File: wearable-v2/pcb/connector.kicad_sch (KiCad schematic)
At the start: 38 parts, among them J1 EXT_1, J11 PNL_1, J12 PNL_2, J13 PNL_3, J14 PNL_4, J2 EXT_2, J3 EXT_3, J4 EXT_4, J7 USB_C_Receptacle_USB2.0, U1 DT1446-04V, U15 TLV751, U2 MCP73831/2-2MC, U3 TCA6408A, U4 FT201XQ

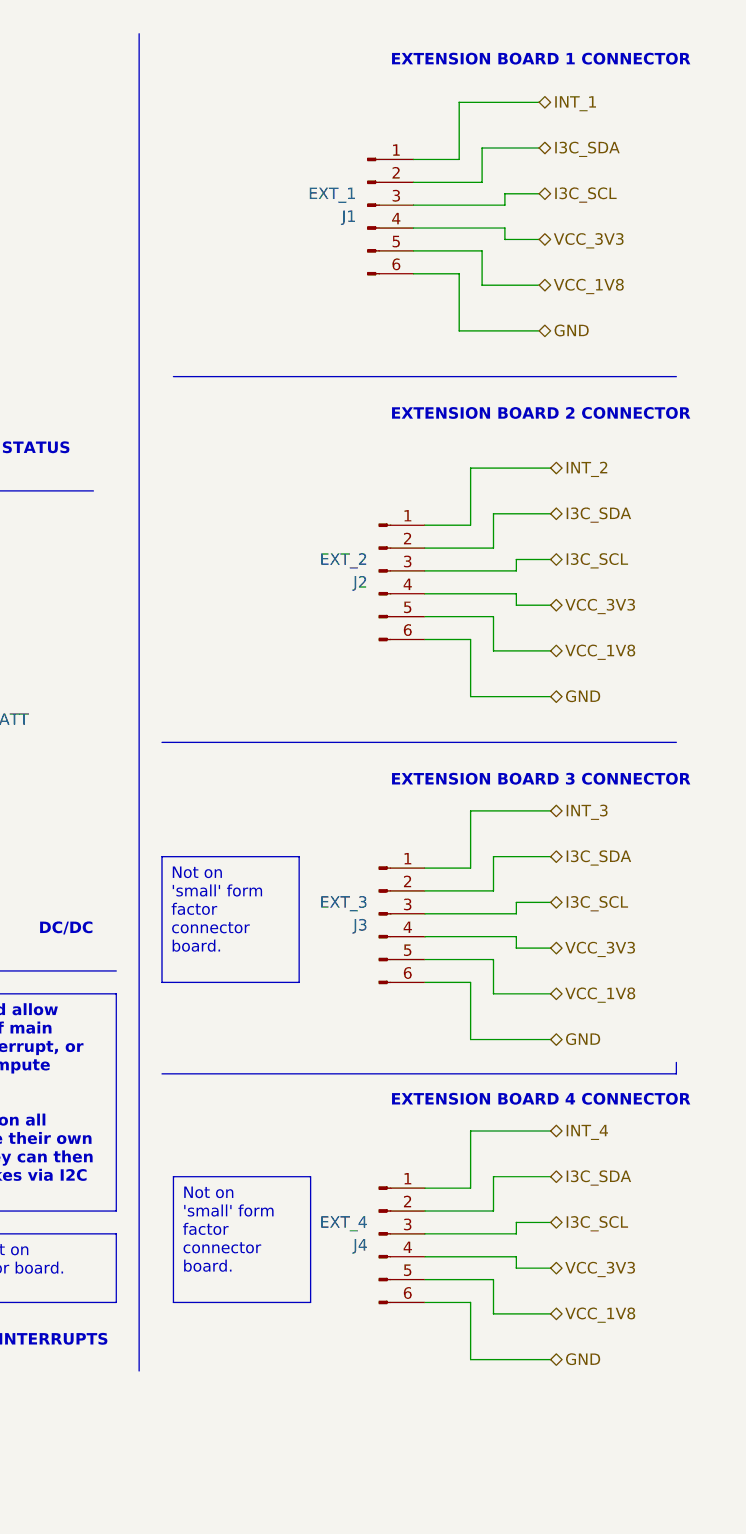
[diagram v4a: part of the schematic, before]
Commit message: Added front connectors on main board
Signed-off-by: Adam Fowler <adam@adamfowler.org>
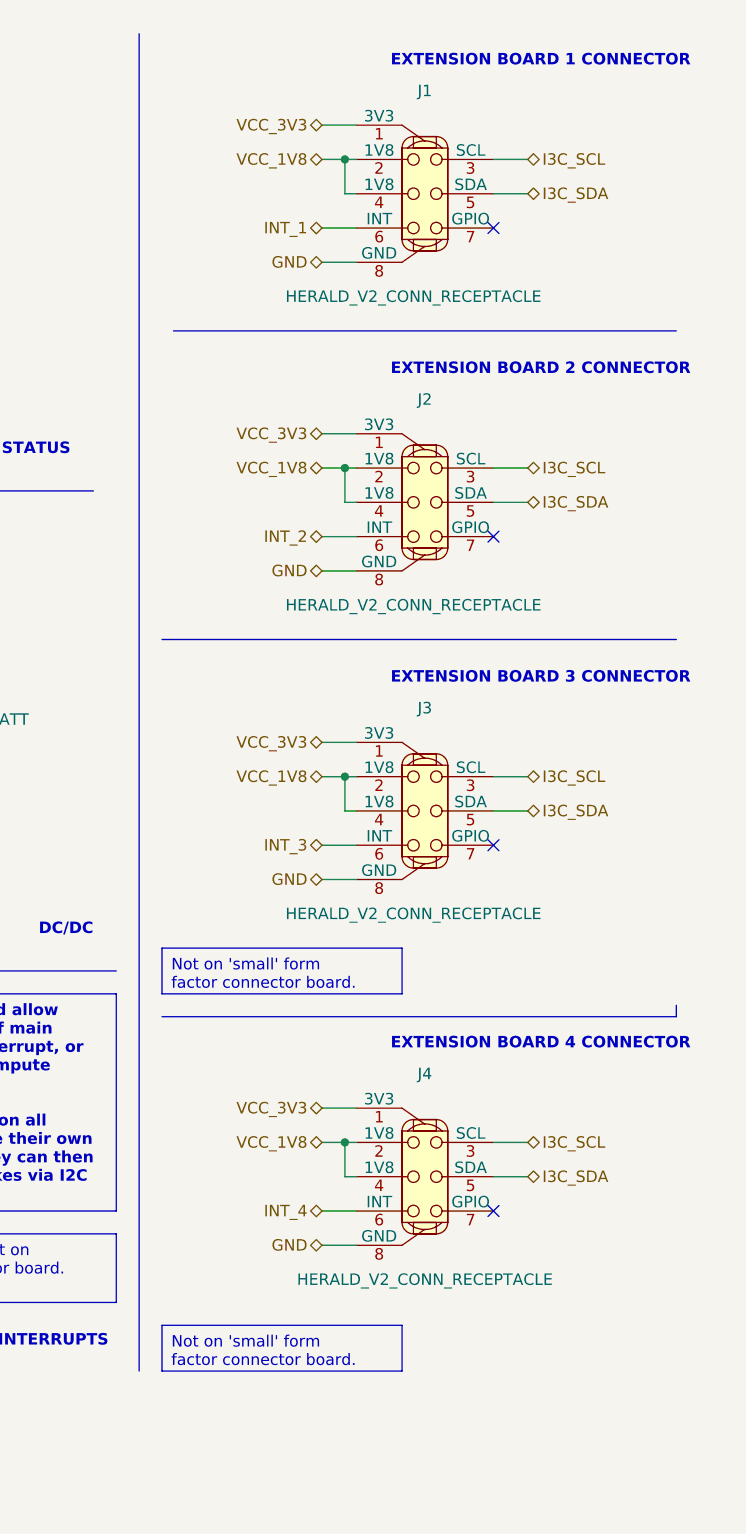
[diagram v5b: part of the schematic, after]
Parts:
- removed J1: EXT_1, symbol Connector:Conn_01x06_Pin
- removed J2: EXT_2, symbol Connector:Conn_01x06_Pin
- removed J3: EXT_3, symbol Connector:Conn_01x06_Pin
- removed J4: EXT_4, symbol Connector:Conn_01x06_Pin
- added J1, J2, J3, J4: HERALD_V2_CONN_RECEPTACLE, Herald:HERALD_V2_CONN_RECEPTACLE, symbol Herald_Extras:HERALD_V2_CONN_RECEPTACLE
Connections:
- net +1V8: now also J1.2 (1V8), J1.4 (1V8), J2.2 (1V8), J2.4 (1V8), J3.2 (1V8), J3.4 (1V8), J4.2 (1V8), J4.4 (1V8)
- net GND: now also J1.8 (GND), J2.8 (GND), J3.8 (GND), J4.8 (GND)
- net I3C_SCL: now also J1.3 (SCL), J2.3 (SCL), J3.3 (SCL), J4.3 (SCL)
- net I3C_SDA: now also J1.5 (SDA), J2.5 (SDA), J3.5 (SDA), J4.5 (SDA)
- net INT_1: now also J1.6 (INT)
- net INT_2: now also J2.6 (INT)
- net INT_3: now also J3.6 (INT)
- net INT_4: now also J4.6 (INT)
- net VDD: now also J1.1 (3V3), J2.1 (3V3), J3.1 (3V3), J4.1 (3V3)
- no-connect marks 13 -> 17

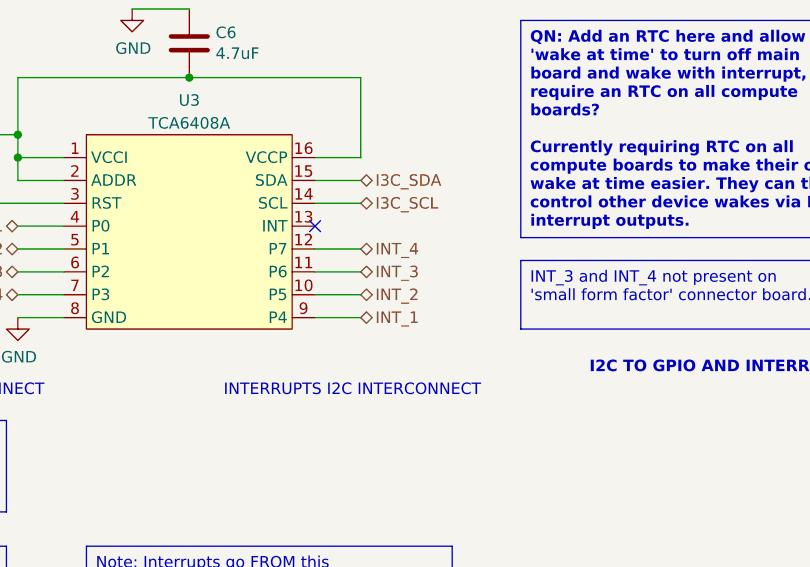
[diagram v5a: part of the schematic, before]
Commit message: All board connectors routed
Connector positions confirmed
Extension board dimensions confirmed to not clash
Signed-off-by: Adam Fowler <adam@adamfowler.org>
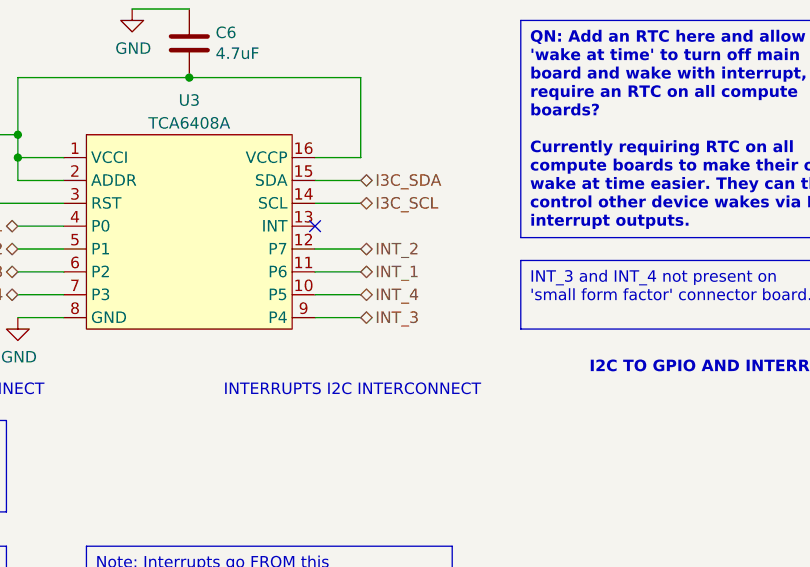
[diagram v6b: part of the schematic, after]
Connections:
- net INT_1: now also U3.11 (P6); no longer U3.9 (P4)
- net INT_2: now also U3.12 (P7); no longer U3.10 (P5)
- net INT_3: now also U3.9 (P4); no longer U3.11 (P6)
- net INT_4: now also U3.10 (P5); no longer U3.12 (P7)
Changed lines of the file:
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@@
+    (stroke (width 0) (type default))
+  )
+  (wire (pts (xy 158.75 149.86) (xy 163.83 149.86))
     (stroke (width 0) (type default))
   )
@@
     (stroke (width 0) (type default))
   )
+  (wire (pts (xy 158.75 154.94) (xy 163.83 154.94))
+    (stroke (width 0) (type default))
+  )
   (wire (pts (xy 33.02 153.67) (xy 31.75 153.67))
     (stroke (width 0) (type default))
@@
     (stroke (width 0) (type default))
   )
+  (wire (pts (xy 158.75 147.32) (xy 163.83 147.32))
+    (stroke (width 0) (type default))
+  )
   (wire (pts (xy 129.54 99.06) (xy 129.54 96.52))
     (stroke (width 0) (type default))
@@
     (stroke (width 0) (type default))
   )
-  (wire (pts (xy 158.75 147.32) (xy 163.83 147.32))
-    (stroke (width 0) (type default))
-  )
   (wire (pts (xy 76.2 97.79) (xy 76.2 99.06))
     (stroke (width 0) (type default))
@@
     (stroke (width 0) (type default))
   )
-  (wire (pts (xy 158.75 154.94) (xy 163.83 154.94))
-    (stroke (width 0) (type default))
-  )
   (wire (pts (xy 27.94 77.47) (xy 25.4 77.47))
     (stroke (width 0) (type default))
@@
     (stroke (width 0) (type default))
   )
+  (wire (pts (xy 158.75 152.4) (xy 163.83 152.4))
+    (stroke (width 0) (type default))
+  )
   (wire (pts (xy 245.11 63.5) (xy 246.38 63.5))
     (stroke (width 0) (type default))
@@
     (stroke (width 0) (type default))
   )
-  (wire (pts (xy 158.75 152.4) (xy 163.83 152.4))
-    (stroke (width 0) (type default))
-  )
   (wire (pts (xy 15.24 134.62) (xy 33.02 134.62))
     (stroke (width 0) (type default))
@@
   )
   (wire (pts (xy 158.75 87.63) (xy 158.75 88.9))
-    (stroke (width 0) (type default))
-  )
-  (wire (pts (xy 158.75 149.86) (xy 163.83 149.86))
     (stroke (width 0) (type default))
   )
@@
     (effects (font (size 1.27 1.27)) (justify left))
   )
-  (hierarchical_label "INT_1" (shape bidirectional) (at 163.83 154.94 0) (fields_autoplaced)
+  (hierarchical_label "INT_1" (shape bidirectional) (at 163.83 149.86 0) (fields_autoplaced)
     (effects (font (size 1.27 1.27)) (justify left))
   )
@@
     (effects (font (size 1.27 1.27)) (justify left))
   )
-  (hierarchical_label "INT_3" (shape bidirectional) (at 163.83 149.86 0) (fields_autoplaced)
+  (hierarchical_label "INT_3" (shape bidirectional) (at 163.83 154.94 0) (fields_autoplaced)
     (effects (font (size 1.27 1.27)) (justify left))
   )
@@
     (effects (font (size 1.27 1.27)) (justify left))
   )
-  (hierarchical_label "INT_4" (shape bidirectional) (at 163.83 147.32 0) (fields_autoplaced)
+  (hierarchical_label "INT_4" (shape bidirectional) (at 163.83 152.4 0) (fields_autoplaced)
     (effects (font (size 1.27 1.27)) (justify left))
   )
@@
     (effects (font (size 1.27 1.27)) (justify left))
   )
-  (hierarchical_label "INT_2" (shape bidirectional) (at 163.83 152.4 0) (fields_autoplaced)
-    (effects (font (size 1.27 1.27)) (justify left))
-  )
+  (hierarchical_label "INT_2" (shape bidirectional) (at 163.83 147.32 0) (fields_autoplaced)
+    (effects (font (size 1.27 1.27)) (justify left))
+  )

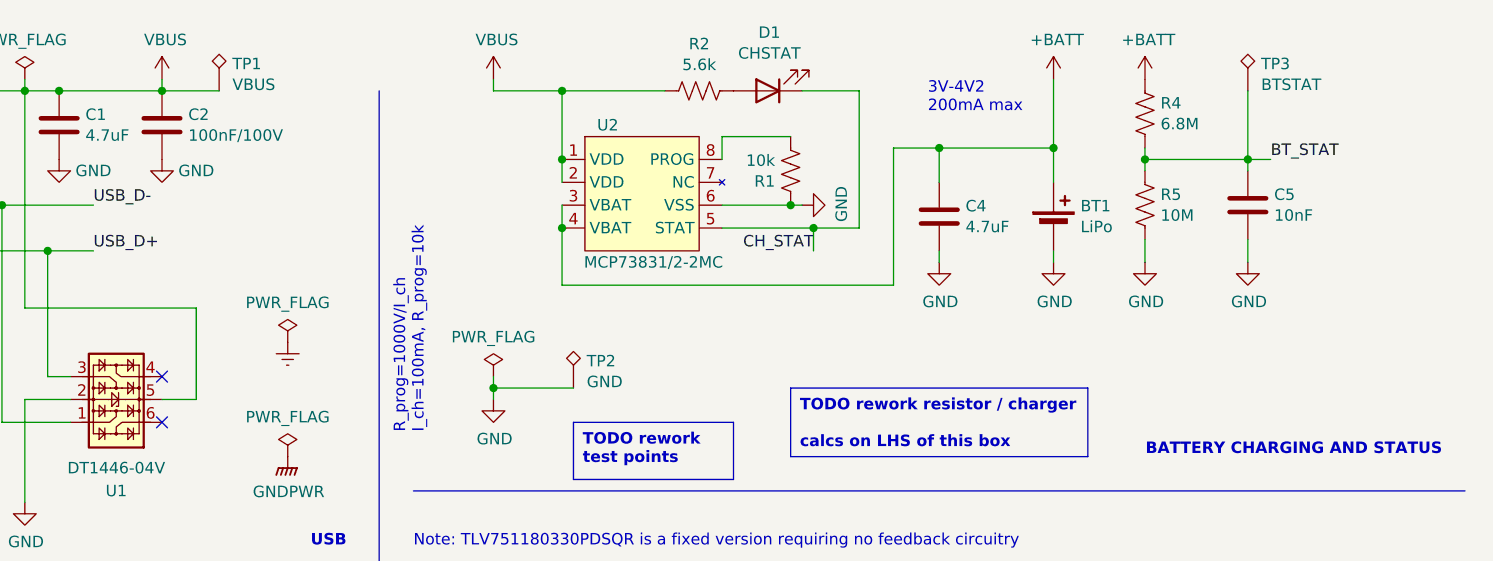
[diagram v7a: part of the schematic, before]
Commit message: Set wider PCB GND tracks and vias
Signed-off-by: Adam Fowler <adam@adamfowler.org>
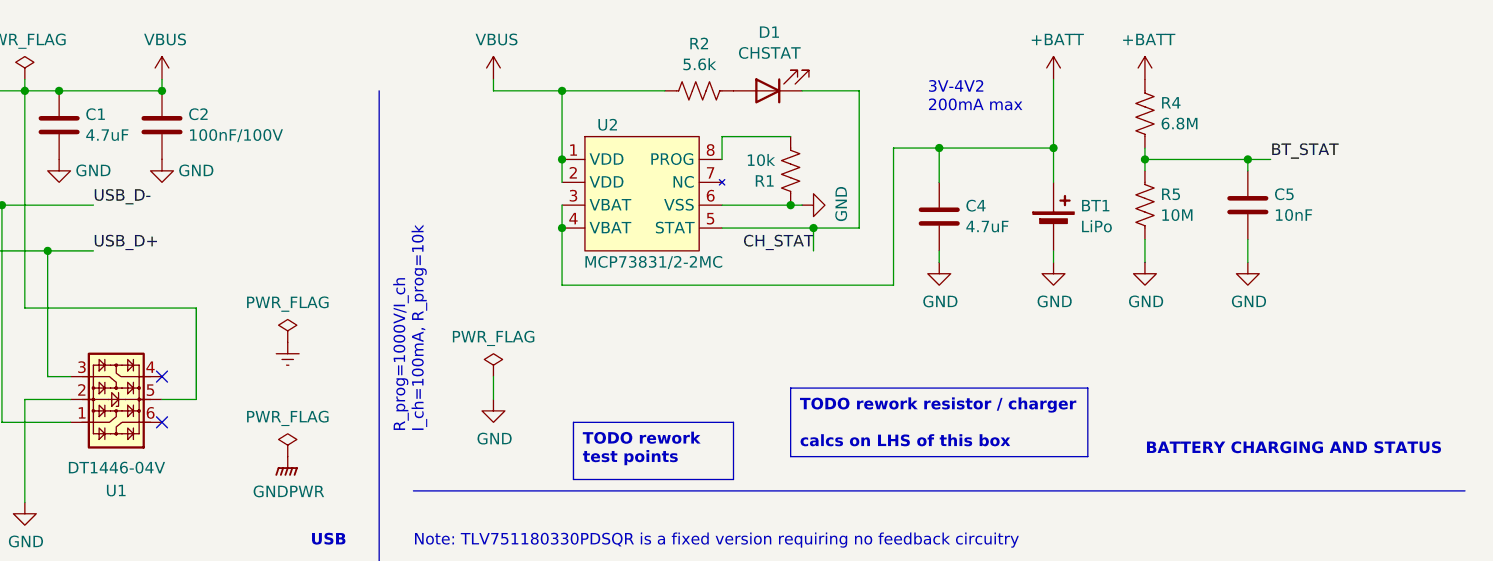
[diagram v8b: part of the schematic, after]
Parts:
- removed TP1: VBUS, TestPoint:TestPoint_Pad_D1.0mm, symbol Connector:TestPoint_Alt
- removed TP2: GND, TestPoint:TestPoint_Pad_D1.0mm, symbol Connector:TestPoint_Alt
- removed TP3: BTSTAT, TestPoint:TestPoint_Pad_D1.0mm, symbol Connector:TestPoint_Alt
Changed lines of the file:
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@@
   (junction (at 245.11 63.5) (diameter 0) (color 0 0 0 0)
-  )
-  (junction (at 109.22 54.61) (diameter 0) (color 0 0 0 0)
   )
   (junction (at 50.8 182.88) (diameter 0) (color 0 0 0 0)
@@
     (stroke (width 0) (type default))
   )
-  (wire (pts (xy 109.22 53.34) (xy 109.22 54.61))
-    (stroke (width 0) (type default))
-  )
   (polyline (pts (xy 100.33 66.04) (xy 217.17 66.04))
     (stroke (width 0) (type default))
@@
     (stroke (width 0) (type default))
   )
-  (wire (pts (xy 78.74 21.59) (xy 72.39 21.59))
-    (stroke (width 0) (type default))
-  )
   (wire (pts (xy 54.61 34.29) (xy 52.07 34.29))
     (stroke (width 0) (type default))
@@
     (stroke (width 0) (type default))
   )
-  (wire (pts (xy 118.11 54.61) (xy 109.22 54.61))
-    (stroke (width 0) (type default))
-  )
   (wire (pts (xy 143.51 34.29) (xy 142.24 34.29))
     (stroke (width 0) (type default))
@@
     (stroke (width 0) (type default))
   )
-  (wire (pts (xy 193.04 21.59) (xy 193.04 29.21))
-    (stroke (width 0) (type default))
-  )
   (wire (pts (xy 39.37 101.6) (xy 41.91 101.6))
     (stroke (width 0) (type default))
@@
     (stroke (width 0) (type default))
   )
-  (wire (pts (xy 109.22 54.61) (xy 109.22 55.88))
+  (wire (pts (xy 109.22 53.34) (xy 109.22 55.88))
     (stroke (width 0) (type default))
   )
@@
         (path "/bdd943b2-035a-4beb-80ad-5c7e84260dde/00000000-0000-0000-0000-000060f1d377"
           (reference "#PWR059") (unit 1)
-        )
-      )
-    )
-  )
-  (symbol (lib_id "Connector:TestPoint_Alt") (at 118.11 54.61 0) (unit 1)
-    (in_bom yes) (on_board yes) (dnp no)
-    (property "Reference" "TP2" (at 119.5832 51.6128 0)
-      (effects (font (size 1.27 1.27)) (justify left))
-    )
-    (property "Value" "GND" (at 119.5832 53.9242 0)
-      (effects (font (size 1.27 1.27)) (justify left))
-    )
-    (property "Footprint" "TestPoint:TestPoint_Pad_D1.0mm" (at 123.19 54.61 0)
-      (effects (font (size 1.27 1.27)) hide)
-    )
-    (property "Datasheet" "~" (at 123.19 54.61 0)
-      (effects (font (size 1.27 1.27)) hide)
-    )
-    (property "Description" "Test point" (at 118.11 54.61 0)
-      (effects (font (size 1.27 1.27)) hide)
-    )
-    (property "MPN" "~" (at 118.11 54.61 0)
-      (effects (font (size 1.27 1.27)) hide)
-    )
-    (pin "1")
-    (instances
-      (project "wearable-v2"
-        (path "/1eb7e8c9-86dc-4f6b-85aa-748b782af952/2bf2cd8a-43d3-474c-96a0-b76bc82af7f4"
-          (reference "TP2") (unit 1)
-        )
-      )
-      (project "wearable"
-        (path "/bdd943b2-035a-4beb-80ad-5c7e84260dde/00000000-0000-0000-0000-000060f1d377"
-          (reference "TP2") (unit 1)
         )
       )
@@
     )
   )
-  (symbol (lib_id "Connector:TestPoint_Alt") (at 193.04 21.59 0) (unit 1)
-    (in_bom yes) (on_board yes) (dnp no)
-    (property "Reference" "TP3" (at 194.5132 18.5928 0)
-      (effects (font (size 1.27 1.27)) (justify left))
-    )
-    (property "Value" "BTSTAT" (at 194.5132 20.9042 0)
-      (effects (font (size 1.27 1.27)) (justify left))
-    )
-    (property "Footprint" "TestPoint:TestPoint_Pad_D1.0mm" (at 198.12 21.59 0)
-      (effects (font (size 1.27 1.27)) hide)
-    )
-    (property "Datasheet" "~" (at 198.12 21.59 0)
-      (effects (font (size 1.27 1.27)) hide)
-    )
-    (property "Description" "Test point" (at 193.04 21.59 0)
-      (effects (font (size 1.27 1.27)) hide)
-    )
-    (property "MPN" "~" (at 193.04 21.59 0)
-      (effects (font (size 1.27 1.27)) hide)
-    )
-    (pin "1")
-    (instances
-      (project "wearable-v2"
-        (path "/1eb7e8c9-86dc-4f6b-85aa-748b782af952/2bf2cd8a-43d3-474c-96a0-b76bc82af7f4"
-          (reference "TP3") (unit 1)
-        )
-      )
-      (project "wearable"
-        (path "/bdd943b2-035a-4beb-80ad-5c7e84260dde/00000000-0000-0000-0000-000060f1d377"
-          (reference "TP22") (unit 1)
-        )
-      )
-    )
-  )
   (symbol (lib_id "Device:FerriteBead") (at 34.29 63.5 0) (unit 1)
     (in_bom yes) (on_board yes) (dnp no)
@@
         )
       )
-    )
-  )
-  (symbol (lib_id "Connector:TestPoint_Alt") (at 78.74 21.59 0) (unit 1)
-    (in_bom yes) (on_board yes) (dnp no)
-    (property "Reference" "TP1" (at 80.2132 18.5928 0)
-      (effects (font (size 1.27 1.27)) (justify left))
-    )
-    (property "Value" "VBUS" (at 80.2132 20.9042 0)
-      (effects (font (size 1.27 1.27)) (justify left))
-    )
-    (property "Footprint" "TestPoint:TestPoint_Pad_D1.0mm" (at 83.82 21.59 0)
-      (effects (font (size 1.27 1.27)) hide)
-    )
-    (property "Datasheet" "~" (at 83.82 21.59 0)
-      (effects (font (size 1.27 1.27)) hide)
-    )
-    (property "Description" "Test point" (at 78.74 21.59 0)
-      (effects (font (size 1.27 1.27)) hide)
-    )
-    (property "MPN" "~" (at 78.74 21.59 0)
-      (effects (font (size 1.27 1.27)) hide)
-    )
-    (pin "1")
-    (instances
-      (project "wearable-v2"
-        (path "/1eb7e8c9-86dc-4f6b-85aa-748b782af952/2bf2cd8a-43d3-474c-96a0-b76bc82af7f4"
-          (reference "TP1") (unit 1)
-        )
-      )
-      (project "wearable"
-        (path "/bdd943b2-035a-4beb-80ad-5c7e84260dde/00000000-0000-0000-0000-000060f1d377"
-          (reference "TP1") (unit 1)
-        )
-      )
